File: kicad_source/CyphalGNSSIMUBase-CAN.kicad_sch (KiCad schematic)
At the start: 30 parts, among them CN1 SM04B-SRSS-TB, CN2 Conn_01x03, CN3 RASPBERRYPI_PICO, SW1 PTS636 SM43 SMTR LFS, U1 M24C64-RMN6TP, U5 MAX3232

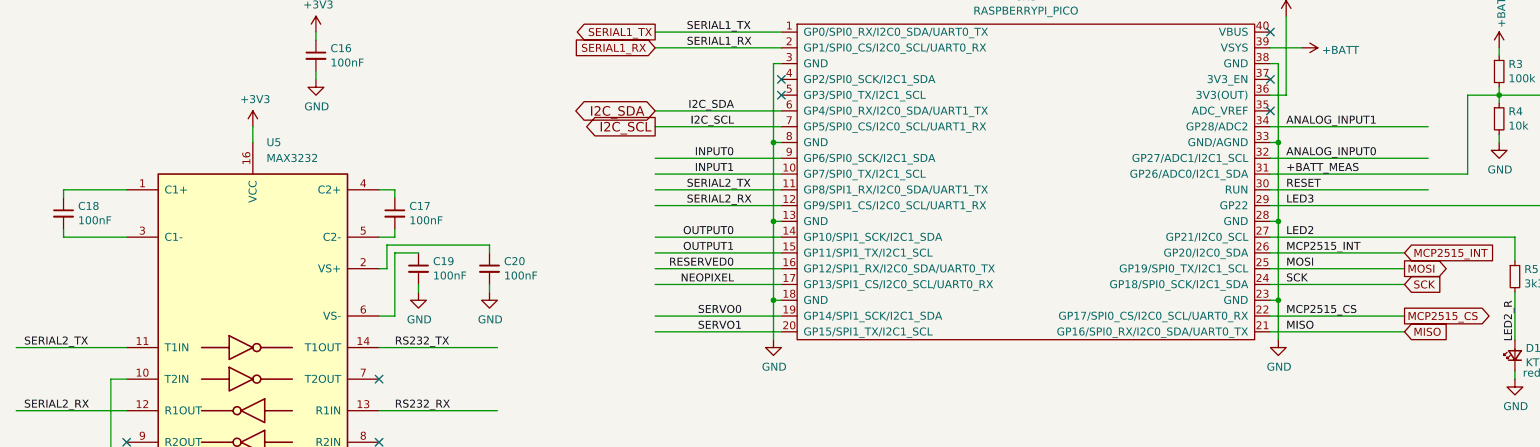
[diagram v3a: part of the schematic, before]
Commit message: connected reset of BNO055 and GNSS module, updated layout
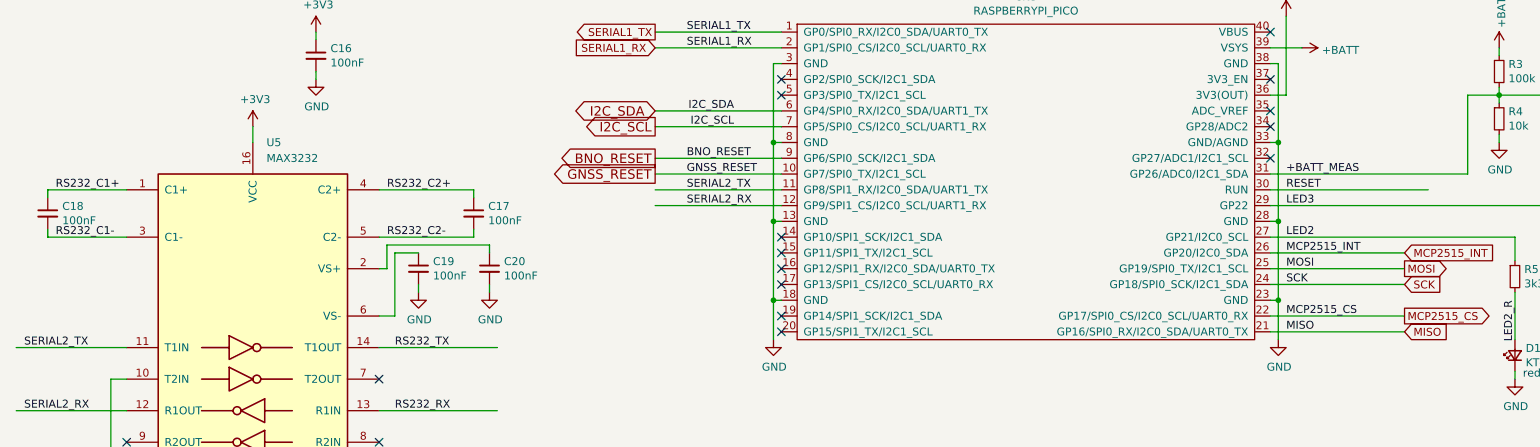
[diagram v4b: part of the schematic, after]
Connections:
- net RS232_C1+: now reaches C18.1, U5.1 (C1+)
- net RS232_C1-: now reaches C18.2, U5.3 (C1-)
- net RS232_C2+: now reaches C17.1, U5.4 (C2+)
- net RS232_C2-: now reaches C17.2, U5.5 (C2-)
- net ANALOG_INPUT0: no longer names the net of CN3.32 (GP27/ADC1/I2C1_SCL)
- net ANALOG_INPUT1: no longer names the net of CN3.34 (GP28/ADC2)
- net INPUT0 renamed BNO_RESET
- net INPUT1 renamed GNSS_RESET
- net NEOPIXEL: no longer names the net of CN3.17 (GP13/SPI1_CS/I2C0_SCL/UART0_RX)
- net OUTPUT0: no longer names the net of CN3.14 (GP10/SPI1_SCK/I2C1_SDA)
- net OUTPUT1: no longer names the net of CN3.15 (GP11/SPI1_TX/I2C1_SCL)
- net RESERVED0: no longer names the net of CN3.16 (GP12/SPI1_RX/I2C0_SDA/UART0_TX)
- net SERVO0: no longer names the net of CN3.19 (GP14/SPI1_SCK/I2C1_SDA)
- net SERVO1: no longer names the net of CN3.20 (GP15/SPI1_TX/I2C1_SCL)
- no-connect marks 12 -> 20
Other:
- moved on the sheet: C17, C18

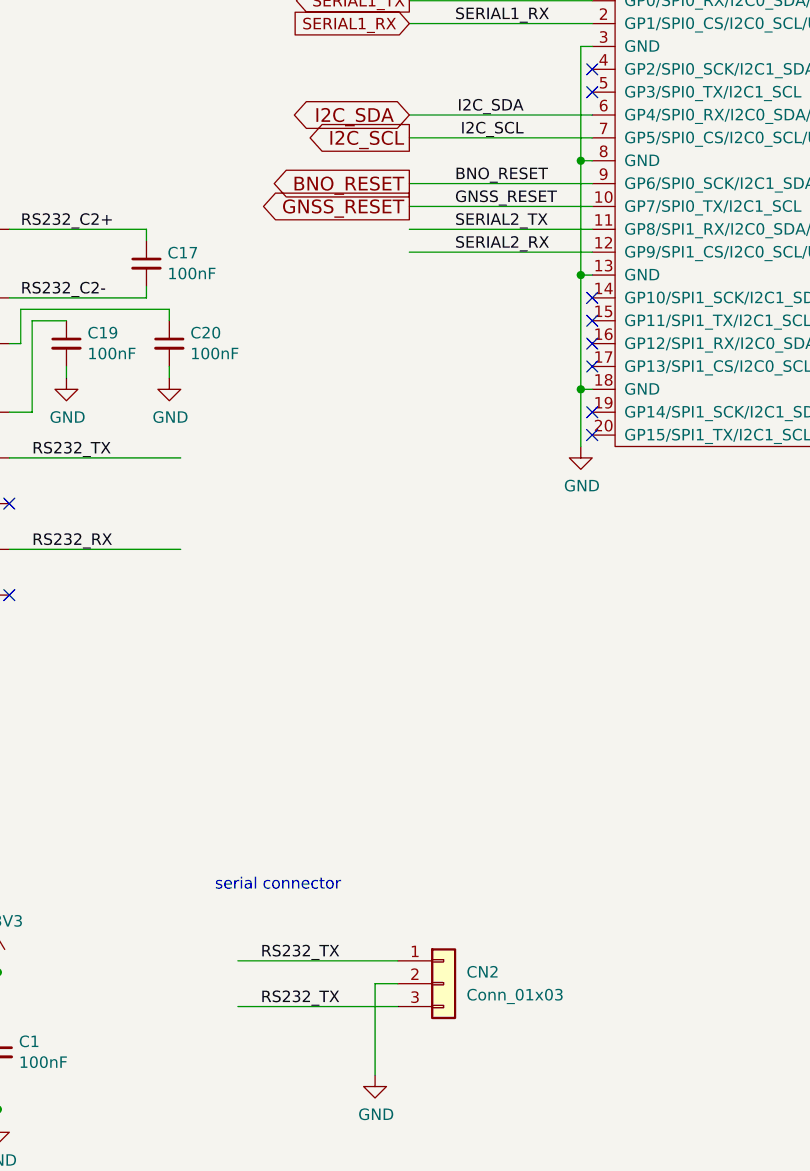
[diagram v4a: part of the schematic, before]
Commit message: updated layout
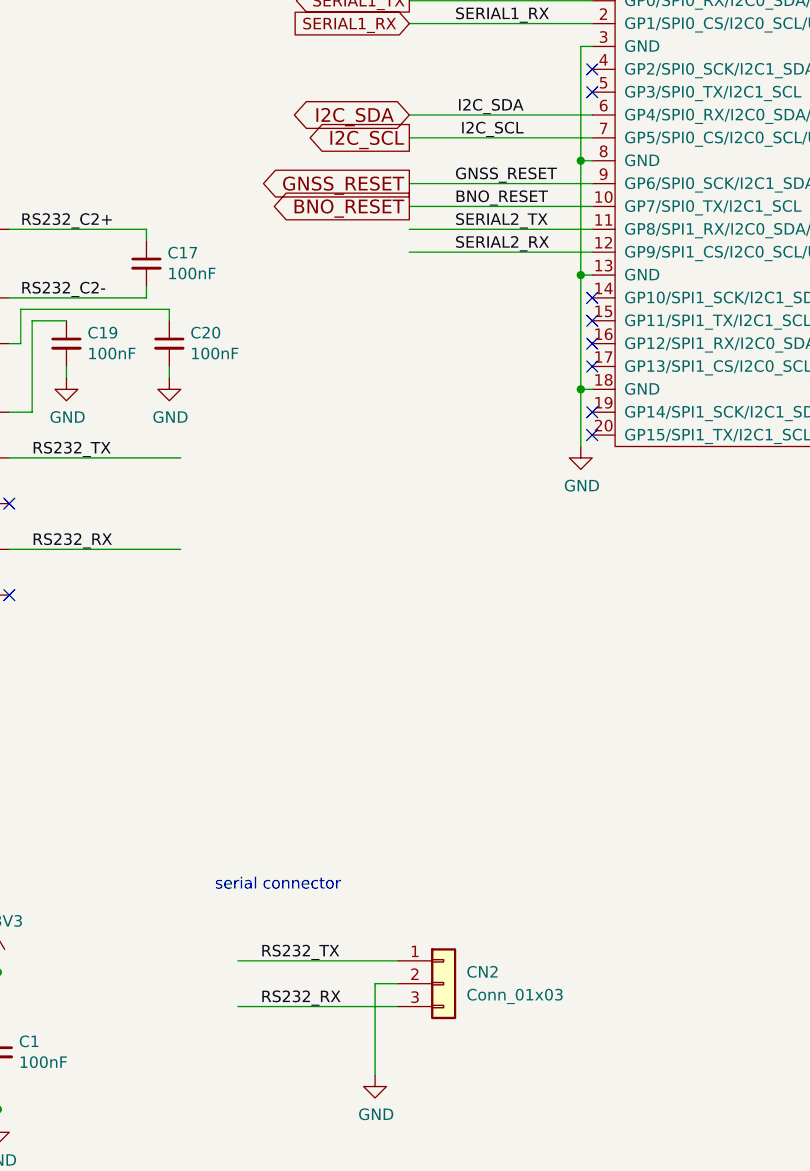
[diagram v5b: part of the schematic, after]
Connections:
- net BNO_RESET: now also CN3.10 (GP7/SPI0_TX/I2C1_SCL); no longer CN3.9 (GP6/SPI0_SCK/I2C1_SDA)
- net GNSS_RESET: now also CN3.9 (GP6/SPI0_SCK/I2C1_SDA); no longer CN3.10 (GP7/SPI0_TX/I2C1_SCL)
- net RS232_RX: now also CN2.3 (Pin_3)
- net RS232_TX: no longer CN2.3 (Pin_3)
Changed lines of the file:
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@@
 	)
 	(label "BNO_RESET"
-		(at 125.73 44.45 0)
+		(at 125.73 46.99 0)
 		(effects
 			(font
@@
 		)
 	)
-	(label "RS232_TX"
+	(label "RS232_RX"
 		(at 104.14 135.89 0)
 		(effects
@@
 	)
 	(label "GNSS_RESET"
-		(at 125.73 46.99 0)
+		(at 125.73 44.45 0)
 		(effects
 			(font
@@
 	(global_label "GNSS_RESET"
 		(shape output)
-		(at 120.65 46.99 180)
+		(at 120.65 44.45 180)
 		(fields_autoplaced yes)
 		(effects
@@
 		)
 		(property "Intersheetrefs" "${INTERSHEET_REFS}"
-			(at 103.7744 46.99 0)
-			(effects
-				(font
-					(size 1.27 1.27)
-				)
-				(justify right)
-				(hide yes)
-			)
-		)
-		(property "Referenzen zwischen Schaltplänen" "${INTERSHEET_REFS}"
-			(at 120.65 49.1921 0)
+			(at 103.7744 44.45 0)
+			(effects
+				(font
+					(size 1.27 1.27)
+				)
+				(justify right)
+				(hide yes)
+			)
+		)
+		(property "Referenzen zwischen Schaltplänen" "${INTERSHEET_REFS}"
+			(at 120.65 46.6521 0)
 			(effects
 				(font
@@
 	(global_label "BNO_RESET"
 		(shape output)
-		(at 120.65 44.45 180)
+		(at 120.65 46.99 180)
 		(fields_autoplaced yes)
 		(effects
@@
 		)
 		(property "Intersheetrefs" "${INTERSHEET_REFS}"
-			(at 105.0806 44.45 0)
-			(effects
-				(font
-					(size 1.27 1.27)
-				)
-				(justify right)
-				(hide yes)
-			)
-		)
-		(property "Referenzen zwischen Schaltplänen" "${INTERSHEET_REFS}"
-			(at 120.65 46.6521 0)
-			(effects
-				(font
+			(at 105.0806 46.99 0)
+			(effects
+				(font
+					(size 1.27 1.27)
+				)
+				(justify right)
+				(hide yes)
+			)
+		)
+		(property "Referenzen zwischen Schaltplänen" "${INTERSHEET_REFS}"
+			(at 120.65 49.1921 0)
+			(effects
+				(font

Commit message: fixed drc errors
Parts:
- CN3: footprint generationmake:RASPI_PICO_SOLDER_Kopie -> generationmake:RASPI_PICO_SOLDER_ONLY
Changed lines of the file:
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@@
 			)
 		)
-		(property "Footprint" "generationmake:RASPI_PICO_SOLDER_Kopie"
+		(property "Footprint" "generationmake:RASPI_PICO_SOLDER_ONLY"
 			(at 180.34 48.26 0)
 			(effects
